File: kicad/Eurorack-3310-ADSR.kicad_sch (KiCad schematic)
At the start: 21 parts, among them J3 Gate In, J4 Trig In

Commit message: Added Schematic Rev 0.1.1
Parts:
- removed R7: 100K, symbol Device:R
- added C6, C7, C8: 100pF, symbol Device:C
- added D3: BAT42, symbol Device:D_Schottky
- added R11, R12, R13, R14, R15, R16, R17, R18, R19, R20, R21, R22, R23, R24: 100K, symbol Device:R
- added R25: 1K, symbol Device:R
- added R8: 30K, symbol Device:R
- added RV1, RV3, RV5, RV7: 100K, symbol Device:R_Potentiometer
- added RV2, RV4, RV6, RV8: 10K, symbol Device:R_Potentiometer
- added TP1: Env out, symbol Connector:TestPoint
- added U2: TL074, symbol Amplifier_Operational:TL074
- added U3: TL072, symbol Amplifier_Operational:TL072
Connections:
- net Trigger_input is gone; now on net 3310_Gate_in: C5.1
- net 3310_Env_out: now also R8.2, TP1.1
- net 3310_Input_current: now also R8.1
- net 3310_Sus_in: now also D3.2 (A), R25.2
- net GND: now also RV1.1, RV2.1, RV3.1, RV4.1, RV5.1, RV6.1, RV7.1, RV8.1, U2.10 (+), U2.3 (+), U2.5 (+), U3.3 (+), U3.5 (+)
- net Attack_input: no longer names the net of R2.1
- net Attack_input: now also C6.2, R13.2, U2.1
- net Decay_input: no longer names the net of R5.1
- net Decay_input: now also C7.2, R15.2, U2.7
- net Release_input: no longer names the net of R9.1
- net Release_input: now also C8.2, R18.2, U2.8
- new net: R21.2, R22.2, R23.1, U3.2 (-)
- new net: R20.1, R23.2, U3.1
- new net: R11.1, RV1.2
- new net: C6.1, R11.2, R12.2, R13.1, U2.2 (-)
- new net: R20.2, R24.1, U3.6 (-)
- new net: R24.2, R25.1, U3.7
- new net: C7.1, R14.2, R15.1, R16.2, U2.6 (-)
- new net: R14.1, RV3.2
- new net: R21.1, RV7.2
- new net: R19.1, RV6.2
- new net: R22.1, RV8.2
- new net: C8.1, R17.2, R18.1, R19.2, U2.9 (-)
- new net: R16.1, RV4.2
- new net: R12.1, RV2.2
- new net: R17.1, RV5.2
- new net +5V: D3.1 (K), RV2.3, RV4.3, RV6.3, RV8.3
- new net Attack CV input: RV1.3
- new net Decay CV input: RV3.3
- new net Release CV input: RV5.3
- new net Sustain CV input: RV7.3
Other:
- note added: "0 to -224mV"
- note added: "0 to 5V"
- note removed: "Attack"
- note removed: "Decay"
- note removed: "Release"
- note removed: "Sustain"
- note removed: "Trig in"
- note removed: "Trig in can be connected to gate in if it is not needed."
- note removed: "VEE to VCC"
- moved on the sheet: C3, C4, C5, J3, J4, R1, R10, R2, R3, R4, R5, R6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

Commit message: Schematic Revision 0.1.1 updated
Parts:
- removed TP1: Env out, symbol Connector:TestPoint
- added C10, C11: 2.2uF, symbol Device:C_Polarized
- added C12, C13: 100nF, symbol Device:C
- added C6, C7: 100pF, symbol Device:C
- added J2: Attack CV In, DIYSynthMNL:AudioJack_3.5mm_long_pads, symbol DIYSynthMNL:PJ3001F
- added J3: Decay CV In, DIYSynthMNL:AudioJack_3.5mm_long_pads, symbol DIYSynthMNL:PJ3001F
- added J5: Release CV In, DIYSynthMNL:AudioJack_3.5mm_long_pads, symbol DIYSynthMNL:PJ3001F
- added J8: Env Out, DIYSynthMNL:AudioJack_3.5mm_long_pads, symbol DIYSynthMNL:PJ3001F
- added R25: 1K, symbol Device:R
- added RV1: 20K, symbol Device:R_Potentiometer_Trim
- added U4: KA78M05_TO252, Package_TO_SOT_SMD:TO-252-2, symbol Regulator_Linear:KA78M05_TO252
- C1: renamed from C3; value 39nF -> 47nF
- C3: renamed from C5; value 3nF -> 2.7nF
- J4: value Trig In -> Sustain CV In
- R2: renamed from R8; value 30K -> 10K
- renumbered C4 to C2, C6 to C4, C7 to C5, D3 to D1, J3 to J1, R15 to R10, R5 to R11, R6 to R12, R16 to R13, R21 to R14, R23 to R15, R24 to R16, R20 to R17, R25 to R18, R22 to R19, R17 to R20, R18 to R21, R9 to R22, R10 to R23, R19 to R24, R4 to R3, R11 to R4, R13 to R5, R2 to R6, R3 to R7, R12 to R8, R14 to R9, RV1 to RV2, RV2 to RV3, RV3 to RV4, RV4 to RV5, RV7 to RV6, RV8 to RV7, RV5 to RV8, RV6 to RV9
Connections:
- net +12V: now also U2.4 (V+), U3.8 (V+), C10.1, C12.1, C13.1, U4.1 (VI)
- net +5V: now also C11.1, U4.3 (VO)
- net -12V: now also U2.11 (V-), U3.4 (V-), C12.2, C13.2
- net 3310_Env_out: now also U2.12 (+), RV1.2, RV1.3; no longer R2.2
- net 3310_Gate_in: now also J1.T
- net Attack CV input: now also J2.T
- net Decay CV input: now also J3.T
- net GND: now also C10.2, C11.2, J2.S, J3.S, J5.S, J8.S, U4.2 (GND)
- net Release CV input: now also J5.T
- net Sustain CV input: now also J4.T
- net at R14.2, R15.1, R19.2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: now also C6.1
- net at R15.2, R17.1, U3.1: now also C6.2
- net at R16.1, R17.2, U3.6 (-): now also C7.1
- net at R16.2, R18.1, U3.7: now also C7.2
- net at U2.13 (-): now also U2.14, R25.1
- new net: J8.T, R25.2
- new net: R2.2, RV1.1
- no-connect marks 8 -> 14
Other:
- note added: "Core"
- note added: "Input Amplitude"
- note added: "Inputs"
- note added: "Level/Offset Level"
- note added: "Output"
- note added: "Power"
- note removed: "Gate in"
- moved on the sheet: C1, C2, C3, C4, C5, C8, C?, D1, D?, J1, J?, R1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

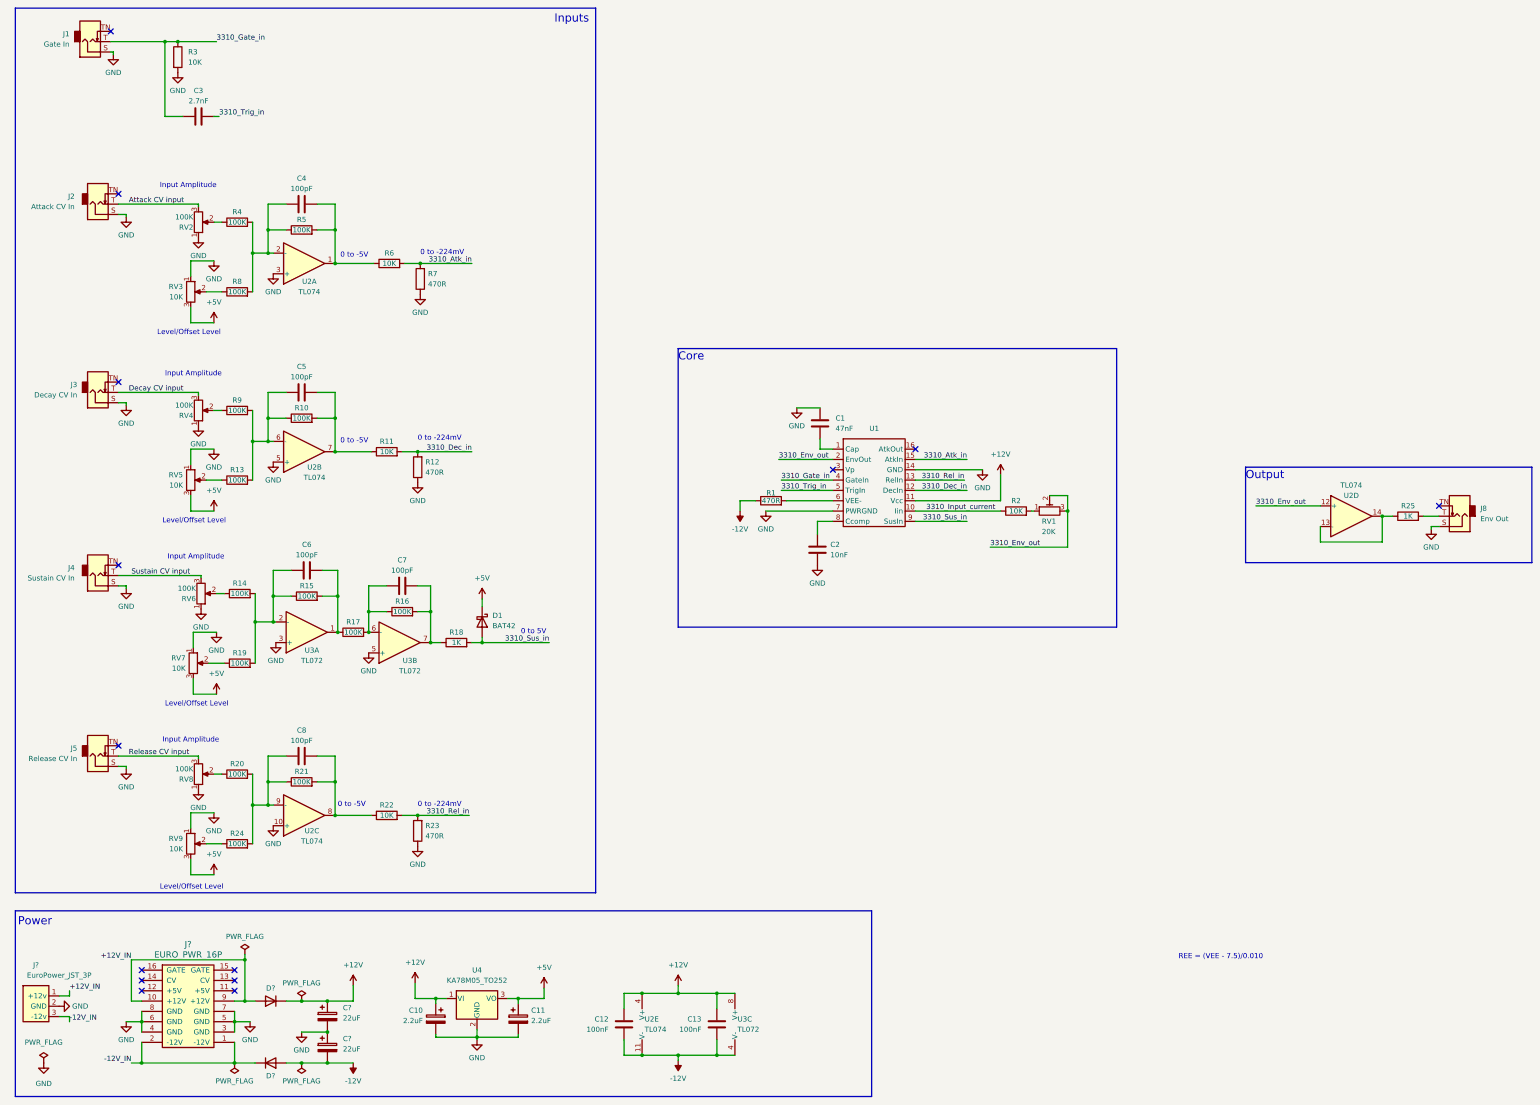
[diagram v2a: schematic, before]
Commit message: Added schematic rev 0.1.2
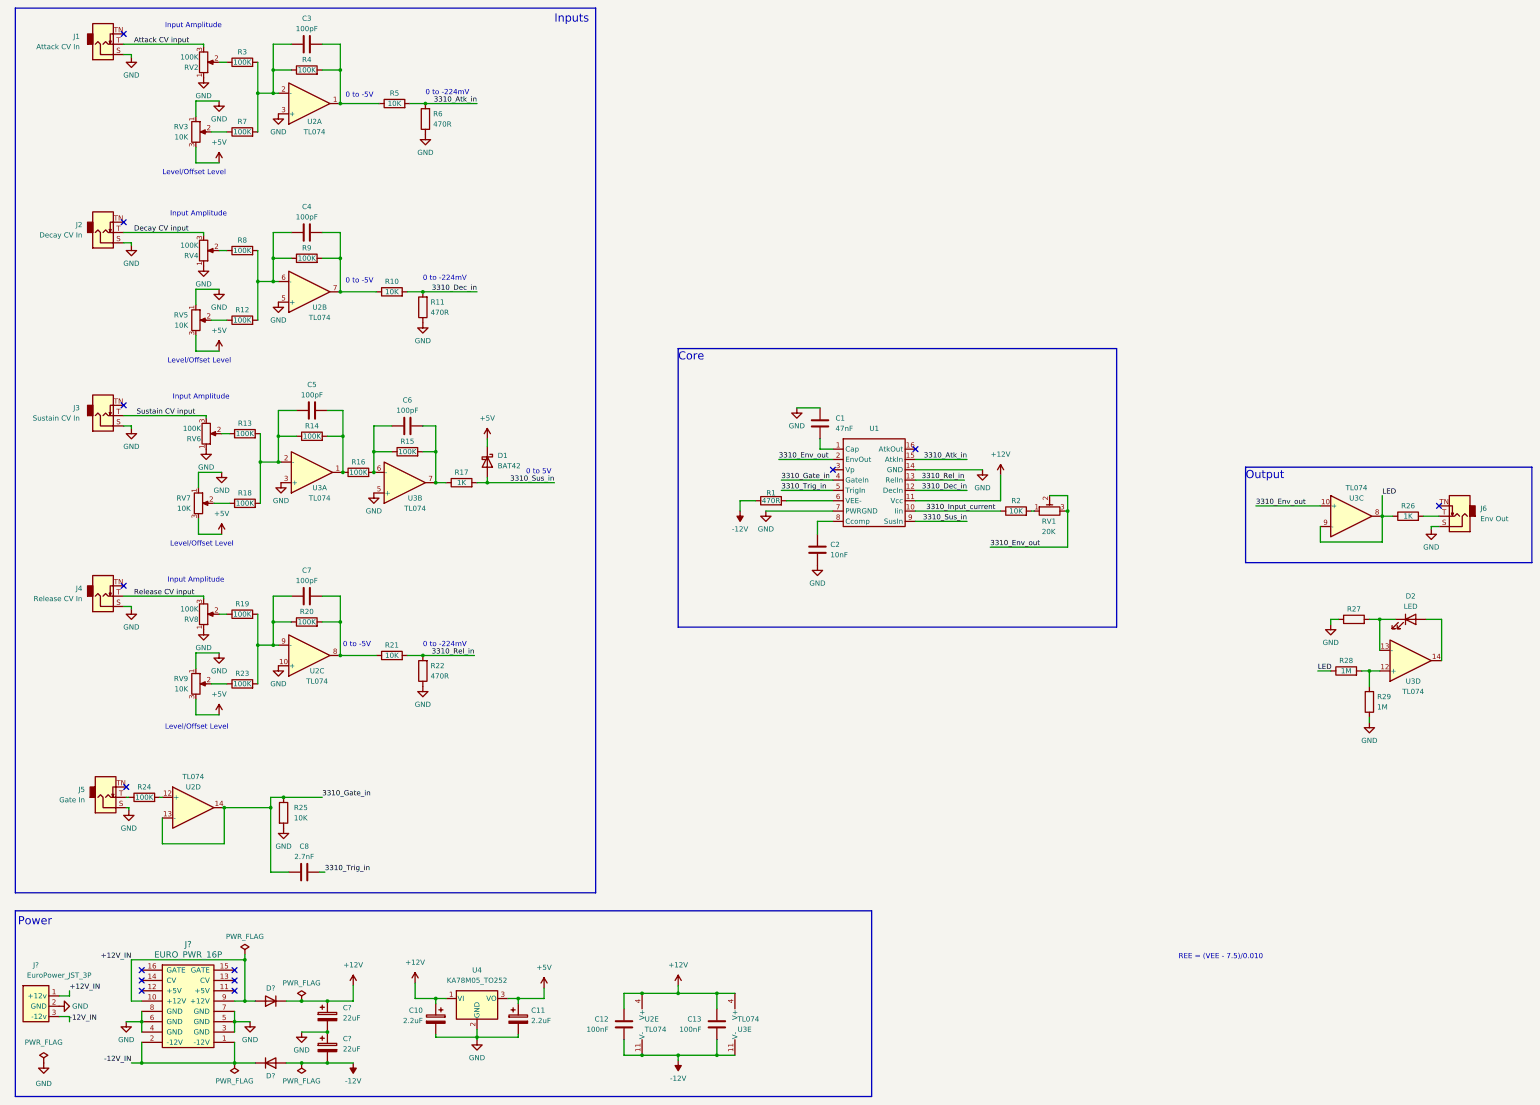
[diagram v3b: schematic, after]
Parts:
- removed U3: TL072, symbol Amplifier_Operational:TL072
- added D2: LED, symbol Device:LED
- added R24: 100K, symbol Device:R
- added R27: ~, symbol Device:R
- added R28, R29: 1M, symbol Device:R
- added U3: TL074, symbol Amplifier_Operational:TL074
- renumbered C4 to C3, C5 to C4, C6 to C5, C7 to C6, C8 to C7, C3 to C8, J2 to J1, J3 to J2, J4 to J3, J5 to J4, J1 to J5, J8 to J6, R11 to R10, R12 to R11, R13 to R12, R14 to R13, R15 to R14, R16 to R15, R17 to R16, R18 to R17, R19 to R18, R20 to R19, R21 to R20, R22 to R21, R23 to R22, R24 to R23, R3 to R25, R25 to R26, R4 to R3, R5 to R4, R6 to R5, R7 to R6, R8 to R7, R9 to R8, R10 to R9
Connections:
- net +12V: now also U3.4 (V+)
- net -12V: now also U3.11 (V-)
- net 3310_Env_out: now also U3.10 (+); no longer U2.12 (+)
- net 3310_Gate_in: now also U2.13 (-), U2.14; no longer J5.T
- net GND: now also R27.1, R29.1, U3.3 (+), U3.5 (+)
- net at C5.1, R13.2, R14.1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: now also U3.2 (-)
- net at C5.2, R14.2, R16.1: now also U3.1
- net at C6.1, R15.1, R16.2: now also U3.6 (-)
- net at C6.2, R15.2, R17.1: now also U3.7
- new net: D2.1 (K), R27.2, U3.13 (-)
- new net: J5.T, R24.1
- new net: R24.2, U2.12 (+)
- new net: R28.2, R29.2, U3.12 (+)
- new net: D2.2 (A), U3.14
- new net LED: R26.1, R28.1, U3.8, U3.9 (-)
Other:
- moved on the sheet: C3, C4, C5, C6, C7, C8, D1, J1, J2, J3, J4, J5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

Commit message: Add schematic rev 0.1.4
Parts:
- added R30: 10K, symbol Device:R
- R2: value 10K -> 16K
- R27: value ~ -> 1K
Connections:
- net GND: now also R30.1
- net at J5.TN: now also R30.2
- no-connect marks 14 -> 13
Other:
- note added: "Rev 0.1.3 Changed R2 to from 10K to 16K. Add value to R27 (1K). Add R30 to prevent input from floating."
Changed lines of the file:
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@@
     (title "Eurorack AS3310 ADSR")
     (date "2024-02-13")
-    (rev "0.1.2")
+    (rev "0.1.3")
     (company "DIYSynthMNL")
     (comment 1 "This version is a prototype")
@@
   (no_connect (at 215.265 128.905))
   (no_connect (at 364.49 137.795))
-  (no_connect (at 41.275 207.01))
   (no_connect (at 45.085 257.175))
   (no_connect (at 40.64 113.03))
@@
     (stroke (width 0) (type default))
   )
+  (wire (pts (xy 41.275 194.31) (xy 49.53 194.31))
+    (stroke (width 0) (type default))
+  )
   (wire (pts (xy 74.295 120.015) (xy 74.295 127))
     (stroke (width 0) (type default))
@@
     (stroke (width 0) (type default))
   )
+  (wire (pts (xy 49.53 194.31) (xy 49.53 196.215))
+    (stroke (width 0) (type default))
+  )
   (wire (pts (xy 73.66 82.55) (xy 73.66 92.075))
     (stroke (width 0) (type default))
   )
+  (wire (pts (xy 41.275 201.93) (xy 41.275 207.01))
+    (stroke (width 0) (type default))
+  )
   (wire (pts (xy 45.085 264.795) (xy 45.085 267.335))
     (stroke (width 0) (type default))
@@
   )
   (text "0 to -224mV" (at 114.3 172.72 0)
+    (effects (font (size 1.27 1.27)) (justify left bottom))
+  )
+  (text "Rev 0.1.3\nChanged R2 to from 10K to 16K.\nAdd value to R27 (1K).\nAdd R30 to prevent input from floating."
+    (at 340.36 249.555 0)
     (effects (font (size 1.27 1.27)) (justify left bottom))
   )
@@
     )
   )
+  (symbol (lib_id "Device:R") (at 41.275 198.12 0) (unit 1)
+    (in_bom yes) (on_board yes) (dnp no)
+    (property "Reference" "R30" (at 36.195 194.945 0)
+      (effects (font (size 1.27 1.27)) (justify left))
+    )
+    (property "Value" "10K" (at 41.275 200.025 90)
+      (effects (font (size 1.27 1.27)) (justify left))
+    )
+    (property "Footprint" "" (at 39.497 198.12 90)
+      (effects (font (size 1.27 1.27)) hide)
+    )
+    (property "Datasheet" "~" (at 41.275 198.12 0)
+      (effects (font (size 1.27 1.27)) hide)
+    )
+    (pin "2")
+    (pin "1")
+    (instances
+      (project "Eurorack-3310-ADSR"
+        (path "/4d8fa7b9-eea2-4c56-998f-1965b20bb5fa"
+          (reference "R30") (unit 1)
+        )
+      )
+    )
+  )
   (symbol (lib_id "Device:R") (at 69.85 28.575 90) (unit 1)
     (in_bom yes) (on_board yes) (dnp no)
@@
       (effects (font (size 1.27 1.27)))
     )
-    (property "Value" "~" (at 343.535 165.735 90)
+    (property "Value" "1K" (at 343.535 165.735 90)
       (effects (font (size 1.27 1.27)))
     )
@@
       (effects (font (size 1.27 1.27)))
     )
-    (property "Value" "10K" (at 260.35 139.065 90)
+    (property "Value" "16K" (at 260.35 139.065 90)
       (effects (font (size 1.27 1.27)))
     )
@@
         )
       )
+    )
+  )
+  (symbol (lib_id "power:GND") (at 49.53 196.215 0) (unit 1)
+    (in_bom yes) (on_board yes) (dnp no) (fields_autoplaced)
+    (property "Reference" "#PWR049" (at 49.53 202.565 0)
+      (effects (font (size 1.27 1.27)) hide)
+    )
+    (property "Value" "GND" (at 49.53 200.66 0)
+      (effects (font (size 1.27 1.27)))
+    )
+    (property "Footprint" "" (at 49.53 196.215 0)
+      (effects (font (size 1.27 1.27)) hide)
+    )
+    (property "Datasheet" "" (at 49.53 196.215 0)
+      (effects (font (size 1.27 1.27)) hide)
+    )
+    (pin "1")
+    (instances
+      (project "Eurorack-3310-ADSR"
+        (path "/4d8fa7b9-eea2-4c56-998f-1965b20bb5fa"
+          (reference "#PWR049") (unit 1)
+        )
+      )
